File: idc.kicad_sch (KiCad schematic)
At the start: 2 parts, among them J1 icd

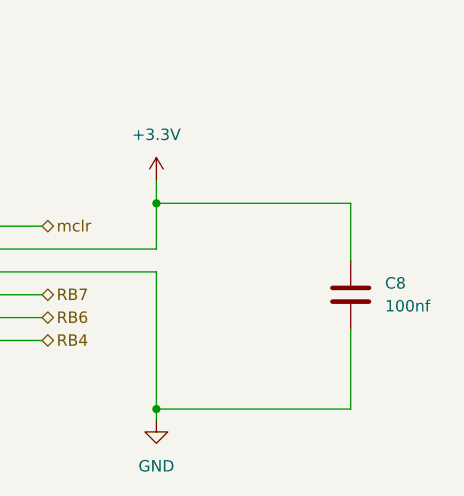
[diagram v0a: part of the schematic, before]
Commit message: feat: PCB layout updates, schematic changes, fp-lib-table config
- cnc_pic32.kicad_pcb: component repositioning, board outline, text formatting
- cnc_pic32.kicad_prl/pro: project settings updates
- fp-lib-table: add Library path to Library.pretty
- mcu.kicad_sch: PIC32 pin configuration updates
- zigbee.kicad_sch: MRF24J40 module updates
- oscilator.kicad_sch: crystal configuration
- power.kicad_sch/power_ft232.kicad_sch: power supply updates
- oled.kicad_sch: OLED display connections
- idc.kicad_sch: IDC connector updates
- osc_ft232.kicad_sch: FT232 crystal
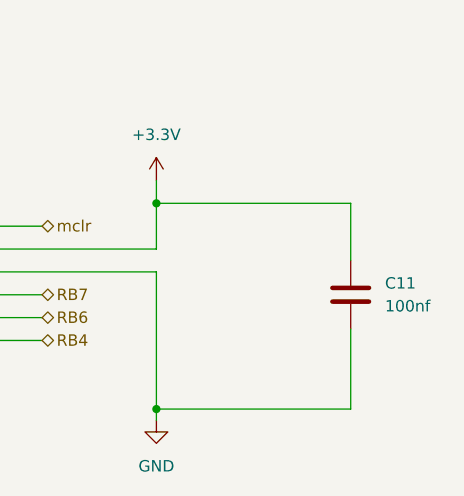
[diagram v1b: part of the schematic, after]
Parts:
- renumbered C8 to C11
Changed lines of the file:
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@@
 		(dnp no)
 		(fields_autoplaced yes)
-		(property "Reference" "#PWR04"
+		(property "Reference" "#PWR06"
 			(at 179.07 67.31 0)
 			(hide yes)
@@
 			(project "cnc_pic32"
 				(path "/13dbfc1f-be47-44ca-9042-3d6a9a657d7d/623622a4-6618-4850-ab50-b533a9bbea15"
-					(reference "#PWR04")
+					(reference "#PWR06")
 					(unit 1)
 				)
@@
 		(dnp no)
 		(fields_autoplaced yes)
-		(property "Reference" "C8"
+		(property "Reference" "C11"
 			(at 204.47 74.9299 0)
 			(show_name no)
@@
 			(project "cnc_pic32"
 				(path "/13dbfc1f-be47-44ca-9042-3d6a9a657d7d/623622a4-6618-4850-ab50-b533a9bbea15"
-					(reference "C8")
+					(reference "C11")
 					(unit 1)
 				)
@@
 		(dnp no)
 		(fields_autoplaced yes)
-		(property "Reference" "#PWR05"
+		(property "Reference" "#PWR07"
 			(at 179.07 96.52 0)
 			(hide yes)
@@
 			(project "cnc_pic32"
 				(path "/13dbfc1f-be47-44ca-9042-3d6a9a657d7d/623622a4-6618-4850-ab50-b533a9bbea15"
-					(reference "#PWR05")
+					(reference "#PWR07")
 					(unit 1)
 				)

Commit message: fix: unify +3.3V to +3V3 across all schematics and PCB
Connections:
- net +3.3V: no longer names the net of C11.1, J1.2 (Pin_2)
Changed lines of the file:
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@@
 	)
 	(symbol
-		(lib_id "power:+3.3V")
+		(lib_id "power:+3V3")
 		(at 179.07 63.5 0)
 		(unit 1)
@@
 			)
 		)
-		(property "Value" "+3.3V"
+		(property "Value" "+3V3"
 			(at 179.07 58.42 0)
 			(show_name no)

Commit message: feat: integrate zigbee sheet + R 0603→0805 footprint update
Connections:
- net +3.3V: now reaches C11.1, J1.2 (Pin_2)
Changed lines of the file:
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@@
 	)
 	(symbol
-		(lib_id "power:+3V3")
+		(lib_id "power:+3.3V")
 		(at 179.07 63.5 0)
 		(unit 1)
@@
 			)
 		)
-		(property "Value" "+3V3"
+		(property "Value" "+3.3V"
 			(at 179.07 58.42 0)
 			(show_name no)

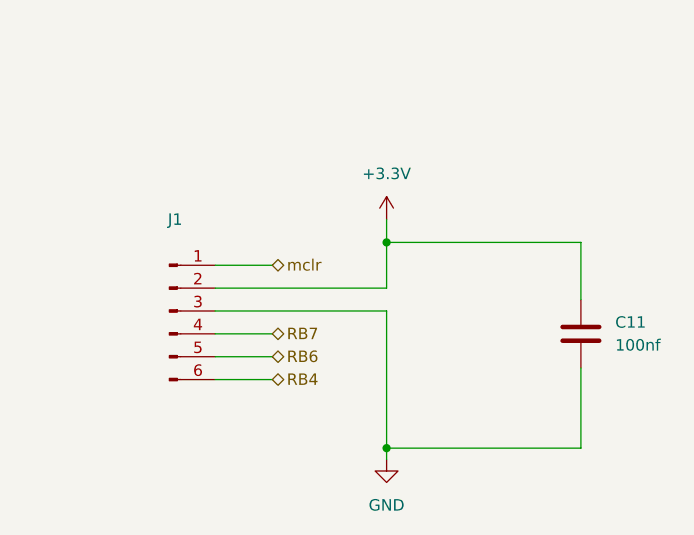
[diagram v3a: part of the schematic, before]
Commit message: feat: 2-layer stackup, bus net class and schematic cleanup
PCB / project
- Reduce board from 4 layers to 2 (F.Cu / B.Cu) for cheaper fabrication
- Add "bus" net class and reorder net class priorities (bus 0, usb_differential 1, ...)

Schematics
- usb_conector_Ft232: add D+ / D-- labels on the USB mini-B data pair
- ft232: add 10K pull-ups, 100nf decoupling and test points on +3.3VA
- tp_ft232: remove solder jumpers JP1/JP2 (TX_Rpi / RX_Rpi now direct)
- Usb_pic32: add C38 100nf decoupling on +5V
- oled: expand connector J25 from 7 to 8 pins
- mcu / idc / power / zigbee / buttons / cnc_pic32: annotation and net cleanup

docs
- Add USB-Mini-B pinout reference images
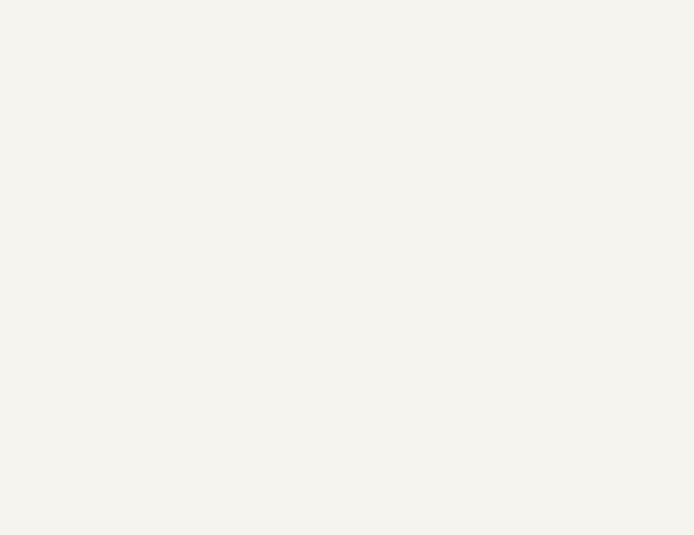
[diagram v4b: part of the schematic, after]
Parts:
- removed C11: 100nf, Capacitor_SMD:C_0805_2012Metric, symbol Device:C
- removed J1: icd, Connector_PinHeader_2.54mm:PinHeader_1x06_P2.54mm_Horizontal, symbol Connector:Conn_01x06_Pin
